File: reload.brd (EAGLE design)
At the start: 49.2 x 30.5 mm, 19 parts, among them IC1 LM358, Q1 BTS117, U1 TL431

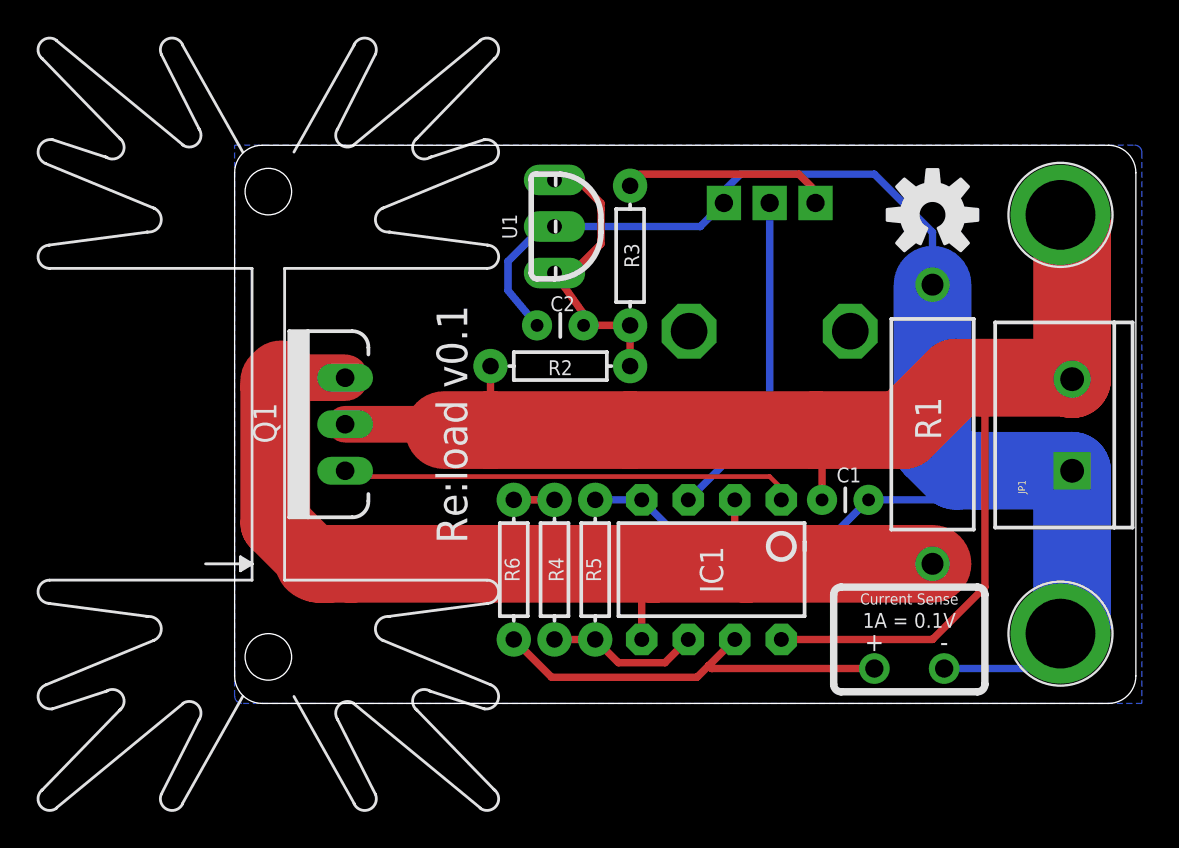
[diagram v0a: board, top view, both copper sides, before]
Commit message: Reworked to use a voltage regulator, added reverse protection diode, other improvements.
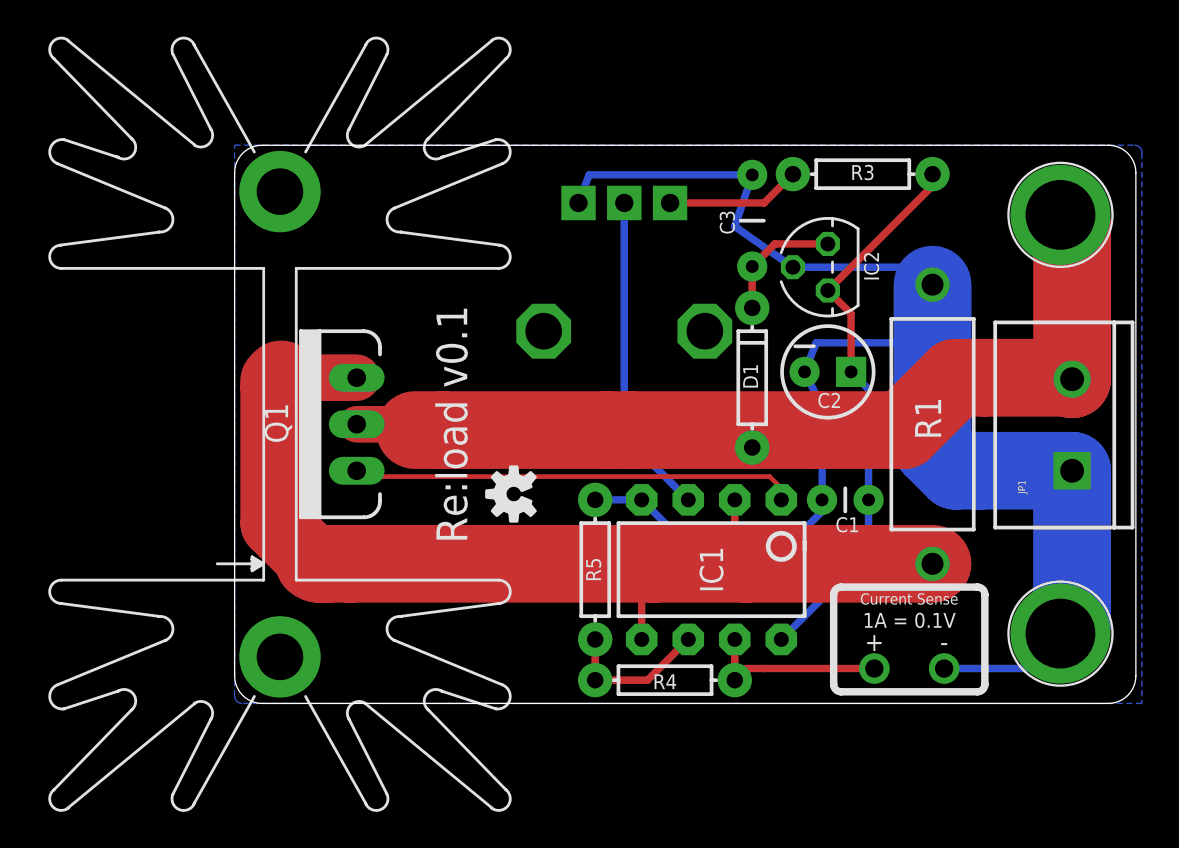
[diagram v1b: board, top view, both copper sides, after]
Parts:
- removed R2: 787, SparkFun-Passives:AXIAL-0.3
- removed R6: 1k 1%, SparkFun-Passives:AXIAL-0.3
- removed U$4: (no value), SparkFun-Aesthetics:OSHW-LOGO-M
- removed U$5: (no value), heatsink:SK129-HOLE
- removed U1: TL431, GuShH:TO-92
- added C3: 1u, SparkFun-Passives:CAP-PTH-5MM
- added D1: (no value), SparkFun-DiscreteSemi:DIODE-1N4148
- added IC2: LP2950Z, linear:TO92
- added KK1: SK129-PAD, nickparts:SK129
- added U$1: (no value), SparkFun-Aesthetics:OSHW-LOGO-S
- C2: value 0.1u -> 10u; device SparkFun-Passives:CAP-PTH-SMALL -> SparkFun-Passives:CPOL-RADIAL-10UF-25V
- R3: value 130k 1% -> 162k
- moved C2 13.6 mm to (32.4, 18.1), turned to 0 degrees
- moved R3 13.5 mm to (34.3, 28.9), turned to 0 degrees
- moved R4 8.53 mm to (23.5, 1.27), turned to 180 degrees
- moved R7 7.94 mm to (21.3, 20.3)
- moved C1 2.54 mm to (34.6, 11.1), turned to 180 degrees
- moved Q1 0.64 mm to (6.67, 15.2)
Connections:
- removed net N$5: C2.1, R2.P$1, R3.P$2, U1.1, U1.3
- removed net N$7: R4.P$1, R6.P$2
- new net 3V: C1.1, C2.1, IC1.8, IC2.1, R3.P$2
- new net N$8: C3.1, D1.C, IC2.3
- net GND: now also C3.2, IC2.2; no longer U1.2
- net IREF: now also R4.P$1; no longer R6.P$1
- net V+: now also D1.A; no longer C1.1, IC1.8, R2.P$2
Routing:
- net 3V: track 0.00 -> 30.7 mm
- net V+: track 81.4 -> 63.0 mm
- net N$5: track 16.6 -> 0.00 mm
- net IREF: track 22.9 -> 10.1 mm
- net N$8: track 0.00 -> 6.90 mm
- net N$3: track 11.6 -> 7.36 mm
- net N$2: track 56.5 -> 59.6 mm
- net N$7: track 2.22 -> 0.00 mm
- net GND: track 90.0 -> 91.3 mm
- net N$1: track 24.8 -> 24.2 mm

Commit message: Added trimpot on back side of board; minor other layout tweaks.
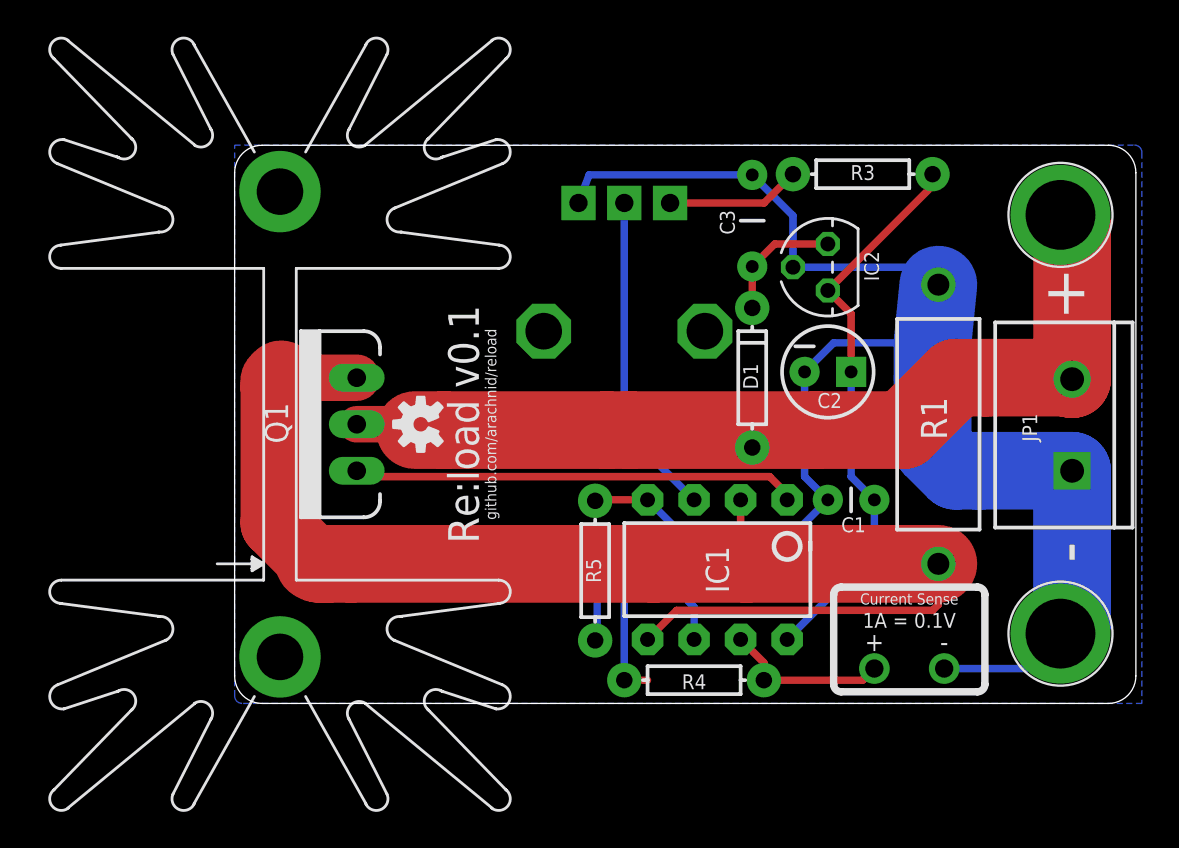
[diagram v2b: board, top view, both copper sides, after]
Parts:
- added R2: 1k, nickparts:TRIMPOT-3MM-2
- IC1: value LM358 -> LP2950
- R4, R5: value 1k 1% -> 10k 1%
- moved U$1 6.35 mm to (10.2, 15.2)
- moved R4 1.59 mm to (25.1, 1.27)
- moved IC1 0.32 mm to (26.4, 7.30)
- moved C1 0.32 mm to (34.9, 11.1)
- moved R1 0.32 mm to (38.4, 15.2)
- moved R5 0.05 mm to (19.7, 7.25)
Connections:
- new net N$5: IC1.6, R2.2
- new net N$7: R2.3, R4.P$2
- net N$6: now also R2.1; no longer IC1.6, R4.P$2
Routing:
- net N$2: track 59.6 -> 76.7 mm
- net N$7: track 0.00 -> 8.92 mm
- net N$6: track 8.22 -> 2.91 mm
- net N$5: track 0.00 -> 4.66 mm
- net IREF: track 10.1 -> 9.04 mm
- net GND: track 91.3 -> 90.3 mm
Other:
- board text added: "github.com/arachnid/reload"

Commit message: Added a second BoM for 10A version.
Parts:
- IC1: value LP2950 -> MCP6002
- renumbered R7 to R6
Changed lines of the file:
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@@
 </autorouter>
 <elements>
-<element name="IC1" library="SparkFun-AnalogIC" package="DIP08" value="LP2950" x="26.3525" y="7.3025" smashed="yes" rot="R180">
+<element name="IC1" library="SparkFun-AnalogIC" package="DIP08" value="MCP6002" x="26.3525" y="7.3025" smashed="yes" rot="R180">
 <attribute name="NAME" x="25.7175" y="7.3025" size="1.27" layer="25" ratio="10" rot="R270" align="bottom-center"/>
 </element>
@@
 <attribute name="VALUE" x="44.45" y="11.43" size="0.4064" layer="27" rot="R90"/>
 </element>
-<element name="R7" library="SparkFun-Electromechanical" package="ALPS_POT" value="10k" x="21.2725" y="20.32" smashed="yes" rot="R90"/>
+<element name="R6" library="SparkFun-Electromechanical" package="ALPS_POT" value="10k" x="21.2725" y="20.32" smashed="yes" rot="R90"/>
 <element name="R3" library="SparkFun-Passives" package="AXIAL-0.3" value="162k" x="34.29" y="28.8925" smashed="yes">
 <attribute name="NAME" x="34.29" y="28.575" size="0.8128" layer="25" font="vector" align="bottom-center"/>
@@
 <contactref element="R1" pad="P$1"/>
 <contactref element="IC1" pad="4"/>
-<contactref element="R7" pad="P$3"/>
+<contactref element="R6" pad="P$3"/>
 <contactref element="C1" pad="2"/>
 <contactref element="R5" pad="P$2"/>
@@
 </signal>
 <signal name="N$3">
-<contactref element="R7" pad="P$1"/>
+<contactref element="R6" pad="P$1"/>
 <contactref element="R3" pad="P$1"/>
 <wire x1="23.7725" y1="27.32" x2="28.9075" y2="27.32" width="0.4064" layer="1"/>
@@
 </signal>
 <signal name="N$4">
-<contactref element="R7" pad="P$2"/>
+<contactref element="R6" pad="P$2"/>
 <contactref element="IC1" pad="3"/>
 <wire x1="21.2725" y1="27.32" x2="21.2725" y2="14.9225" width="0.4064" layer="16"/>

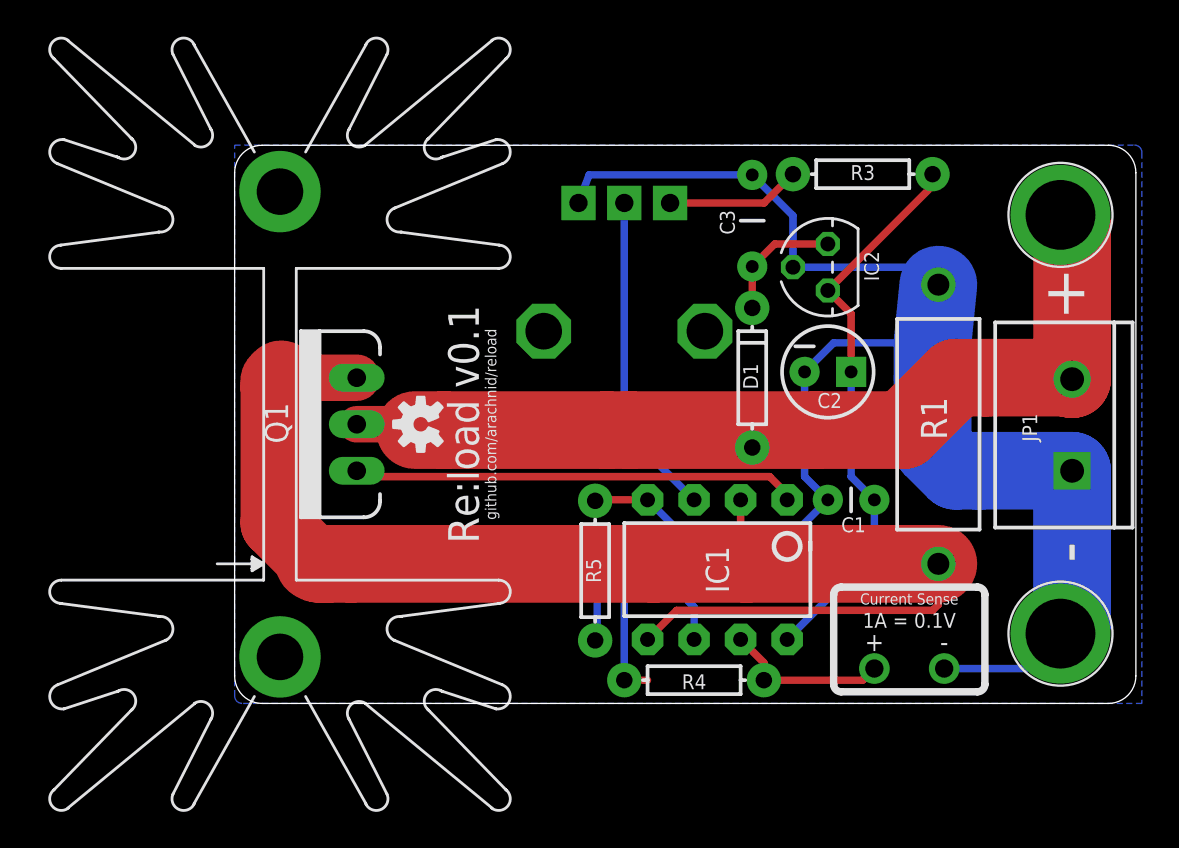
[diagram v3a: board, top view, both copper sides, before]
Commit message: Added series resistor for FET output.
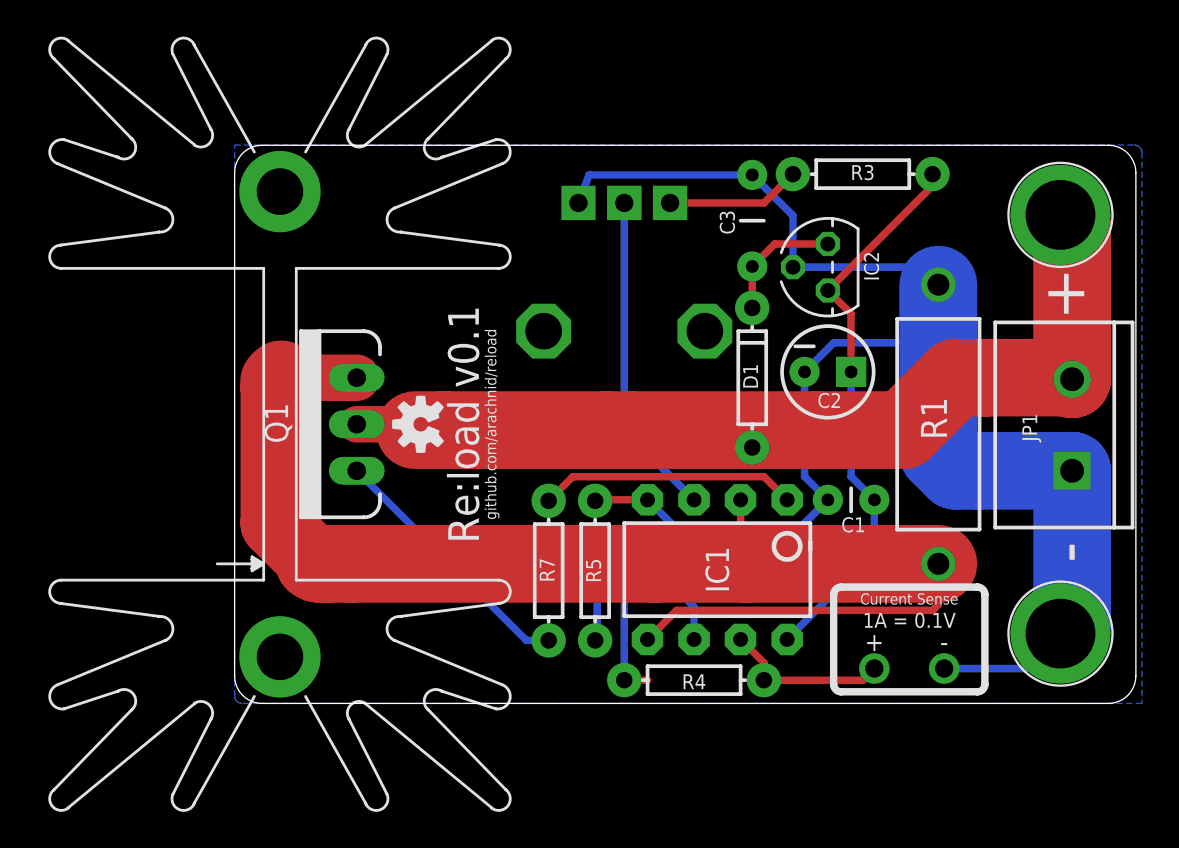
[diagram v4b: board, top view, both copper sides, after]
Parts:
- added R7: 100, SparkFun-Passives:AXIAL-0.3
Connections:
- new net N$9: Q1.1, R7.P$1
- net N$1: now also R7.P$2; no longer Q1.1
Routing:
- net N$9: track 0.00 -> 14.3 mm
- net N$1: track 24.3 -> 14.1 mm
- net GND: track 90.3 -> 89.7 mm
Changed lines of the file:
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@@
 <attribute name="NAME" x="21.1455" y="6.5405" size="0.8128" layer="26" rot="MR90"/>
+</element>
+<element name="R7" library="SparkFun-Passives" package="AXIAL-0.3" value="100" x="17.145" y="7.25" smashed="yes" rot="R90">
+<attribute name="NAME" x="17.4625" y="6.615" size="0.8128" layer="25" font="vector" rot="R90"/>
 </element>
 </elements>
 <signals>
-<signal name="N$1">
-<contactref element="IC1" pad="1"/>
-<contactref element="Q1" pad="1"/>
-<wire x1="30.1625" y1="11.1125" x2="30.1625" y2="11.43" width="0.4064" layer="1"/>
-<wire x1="30.1625" y1="11.43" x2="29.21" y2="12.3825" width="0.4064" layer="1"/>
-<wire x1="29.21" y1="12.3825" x2="6.985" y2="12.3825" width="0.4064" layer="1"/>
-<wire x1="6.985" y1="12.3825" x2="6.6675" y2="12.7" width="0.4064" layer="1"/>
-</signal>
 <signal name="V+">
 <contactref element="Q1" pad="2"/>
@@
 <wire x1="5.08" y1="7.62" x2="4.6133375" y2="7.62" width="4.2418" layer="1"/>
 <wire x1="4.6133375" y1="7.62" x2="4.32596875" y2="7.73903125" width="4.2418" layer="1" curve="-45"/>
-<wire x1="4.32596875" y1="7.73903125" x2="2.2225" y2="9.8425" width="3.81" layer="1"/>
 <wire x1="2.2225" y1="9.8425" x2="2.2225" y2="17.2941625" width="3.81" layer="1"/>
 <wire x1="2.2225" y1="17.2941625" x2="2.34153125" y2="17.58153125" width="3.81" layer="1" curve="-45"/>
@@
 <wire x1="38.4175" y1="5.3975" x2="38.4175" y2="7.62" width="0.4064" layer="1"/>
 <wire x1="27.6225" y1="11.1125" x2="27.6225" y2="7.9375" width="0.4064" layer="1"/>
+<wire x1="4.32596875" y1="7.73903125" x2="2.2225" y2="9.8425" width="3.81" layer="1"/>
 </signal>
 <signal name="GND">
@@
 <wire x1="45.72" y1="12.7" x2="40.64" y2="12.7" width="4.2418" layer="16"/>
 <wire x1="40.64" y1="12.7" x2="39.37" y2="12.7" width="4.2418" layer="16"/>
-<wire x1="39.37" y1="12.7" x2="38.1" y2="13.97" width="4.2418" layer="16"/>
-<wire x1="38.1" y1="13.97" x2="38.1" y2="17.78" width="4.2418" layer="16"/>
-<wire x1="38.1" y1="17.78" x2="38.1" y2="19.685" width="4.2418" layer="16"/>
-<wire x1="38.1" y1="19.685" x2="38.4175" y2="22.86" width="4.2418" layer="16"/>
 <wire x1="45.72" y1="12.7" x2="45.72" y2="4.445" width="4.2418" layer="16"/>
 <wire x1="45.72" y1="4.445" x2="45.085" y2="3.81" width="4.2418" layer="16"/>
@@
 <wire x1="30.48" y1="23.8125" x2="37.1475" y2="23.8125" width="0.4064" layer="16"/>
 <wire x1="37.1475" y1="23.8125" x2="38.4175" y2="22.86" width="0.4064" layer="16"/>
-<wire x1="37.7825" y1="18.0975" x2="38.1" y2="17.78" width="0.4064" layer="16"/>
 <wire x1="28.2575" y1="28.8525" x2="19.3525" y2="28.8525" width="0.4064" layer="16"/>
 <wire x1="19.3525" y1="28.8525" x2="18.7725" y2="27.32" width="0.4064" layer="16"/>
@@
 <wire x1="22.5425" y1="11.1125" x2="19.735" y2="11.1125" width="0.4064" layer="1"/>
 <wire x1="19.735" y1="11.1125" x2="19.6825" y2="11.06" width="0.4064" layer="1"/>
+<wire x1="38.4175" y1="22.86" x2="38.4175" y2="13.6525" width="4.2418" layer="16"/>
+<wire x1="38.4175" y1="13.6525" x2="39.37" y2="12.7" width="4.2418" layer="16"/>
 </signal>
 <signal name="N$3">
@@
 <wire x1="19.79" y1="3.5475" x2="19.6825" y2="3.44" width="0.4064" layer="16"/>
 </signal>
+<signal name="N$1">
+<contactref element="IC1" pad="1"/>
+<contactref element="R7" pad="P$2"/>
+<wire x1="30.1625" y1="11.1125" x2="28.8925" y2="12.3825" width="0.4064" layer="1"/>
+<wire x1="28.8925" y1="12.3825" x2="18.4675" y2="12.3825" width="0.4064" layer="1"/>
+<wire x1="18.4675" y1="12.3825" x2="17.145" y2="11.06" width="0.4064" layer="1"/>
+</signal>
+<signal name="N$9">
+<contactref element="R7" pad="P$1"/>
+<contactref element="Q1" pad="1"/>
+<wire x1="17.145" y1="3.44" x2="15.9275" y2="3.44" width="0.4064" layer="16"/>
+<wire x1="15.9275" y1="3.44" x2="6.6675" y2="12.7" width="0.4064" layer="16"/>
+</signal>
 </signals>

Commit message: Tweaks to schematic.
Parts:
- R6: device SparkFun-Electromechanical:ALPS_POT -> nickparts:ALPS_POT
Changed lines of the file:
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@@
 <attribute name="VALUE" x="44.45" y="11.43" size="0.4064" layer="27" rot="R90"/>
 </element>
-<element name="R6" library="SparkFun-Electromechanical" package="ALPS_POT" value="10k" x="21.2725" y="20.32" smashed="yes" rot="R90"/>
+<element name="R6" library="nickparts" package="ALPS_POT" value="10k" x="21.2725" y="20.32" smashed="yes" rot="R90">
+<attribute name="NAME" x="18.0975" y="15.875" size="1.27" layer="21" rot="R90"/>
+</element>
 <element name="R3" library="SparkFun-Passives" package="AXIAL-0.3" value="162k" x="34.29" y="28.8925" smashed="yes">
 <attribute name="NAME" x="34.29" y="28.575" size="0.8128" layer="25" font="vector" align="bottom-center"/>

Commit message: Improved schematic layout.
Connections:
- net 3V renamed VCC
- net N$2 renamed SENSE
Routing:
- net SENSE: track 76.7 -> 74.5 mm
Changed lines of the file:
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@@
 <wire x1="20.833159375" y1="15.435659375" x2="20.32" y2="14.9225" width="2" layer="1"/>
 </signal>
-<signal name="N$2">
+<signal name="SENSE">
 <contactref element="Q1" pad="3"/>
 <contactref element="R1" pad="P$2"/>
 <contactref element="IC1" pad="2"/>
-<contactref element="IC1" pad="5"/>
 <wire x1="6.35" y1="7.62" x2="22.86" y2="7.62" width="4.2418" layer="1"/>
 <wire x1="22.86" y1="7.62" x2="27.94" y2="7.62" width="4.2418" layer="1"/>
@@
 <wire x1="27.305" y1="8.255" x2="27.94" y2="7.62" width="0.4064" layer="1"/>
 <wire x1="27.6225" y1="7.9375" x2="27.94" y2="7.62" width="0.4064" layer="1"/>
-<wire x1="22.5425" y1="3.4925" x2="24.13" y2="5.08" width="0.4064" layer="1"/>
 <wire x1="24.13" y1="5.08" x2="38.1" y2="5.08" width="0.4064" layer="1"/>
 <wire x1="38.1" y1="5.08" x2="38.4175" y2="5.3975" width="0.4064" layer="1"/>
@@
 <wire x1="27.6225" y1="11.1125" x2="27.6225" y2="7.9375" width="0.4064" layer="1"/>
 <wire x1="4.32596875" y1="7.73903125" x2="2.2225" y2="9.8425" width="3.81" layer="1"/>
+<contactref element="IC1" pad="5"/>
+<wire x1="24.13" y1="5.08" x2="22.5425" y2="3.4925" width="0" layer="19" extent="1-1"/>
 </signal>
 <signal name="GND">
@@
 <wire x1="34.29" y1="1.27" x2="34.925" y2="1.905" width="0.4064" layer="1"/>
 </signal>
-<signal name="3V">
-<contactref element="R3" pad="P$2"/>
-<contactref element="C2" pad="1"/>
-<contactref element="IC1" pad="8"/>
-<contactref element="C1" pad="1"/>
-<contactref element="IC2" pad="1"/>
-<wire x1="38.1" y1="28.8925" x2="38.1" y2="28.2575" width="0.4064" layer="1"/>
-<wire x1="38.1" y1="28.2575" x2="32.385" y2="22.5425" width="0.4064" layer="1"/>
-<wire x1="33.655" y1="18.0975" x2="33.655" y2="21.2725" width="0.4064" layer="1"/>
-<wire x1="33.655" y1="21.2725" x2="32.385" y2="22.5425" width="0.4064" layer="1"/>
-<wire x1="33.655" y1="18.0975" x2="33.655" y2="12.3825" width="0.4064" layer="16"/>
-<wire x1="33.655" y1="12.3825" x2="34.925" y2="11.1125" width="0.4064" layer="16"/>
-<wire x1="34.925" y1="11.1125" x2="34.925" y2="8.255" width="0.4064" layer="16"/>
-<wire x1="34.925" y1="8.255" x2="30.1625" y2="3.4925" width="0.4064" layer="16"/>
-</signal>
 <signal name="N$8">
 <contactref element="D1" pad="C"/>
@@
 <wire x1="15.9275" y1="3.44" x2="6.6675" y2="12.7" width="0.4064" layer="16"/>
 </signal>
+<signal name="VCC">
+<contactref element="R3" pad="P$2"/>
+<contactref element="C2" pad="1"/>
+<contactref element="IC1" pad="8"/>
+<contactref element="C1" pad="1"/>
+<contactref element="IC2" pad="1"/>
+<wire x1="38.1" y1="28.8925" x2="38.1" y2="28.2575" width="0.4064" layer="1"/>
+<wire x1="38.1" y1="28.2575" x2="32.385" y2="22.5425" width="0.4064" layer="1"/>
+<wire x1="33.655" y1="18.0975" x2="33.655" y2="21.2725" width="0.4064" layer="1"/>
+<wire x1="33.655" y1="21.2725" x2="32.385" y2="22.5425" width="0.4064" layer="1"/>
+<wire x1="33.655" y1="18.0975" x2="33.655" y2="12.3825" width="0.4064" layer="16"/>
+<wire x1="33.655" y1="12.3825" x2="34.925" y2="11.1125" width="0.4064" layer="16"/>
+<wire x1="34.925" y1="11.1125" x2="34.925" y2="8.255" width="0.4064" layer="16"/>
+<wire x1="34.925" y1="8.255" x2="30.1625" y2="3.4925" width="0.4064" layer="16"/>
+</signal>
 </signals>
